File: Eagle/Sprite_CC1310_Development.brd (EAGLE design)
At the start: 50 x 50 mm, 81 parts, among them J2 CORTEX_DEBUG_SMD

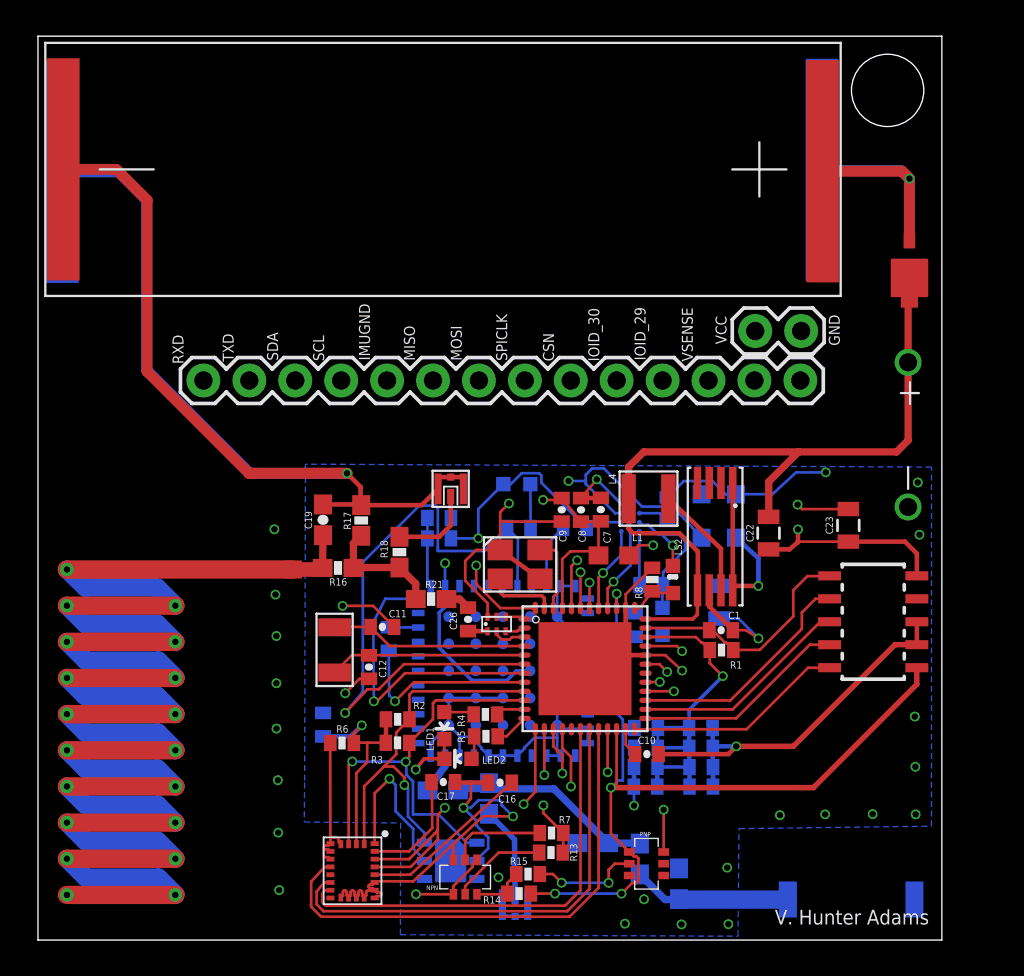
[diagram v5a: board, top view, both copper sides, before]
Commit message: RFQ for BSU, changed matching circuit
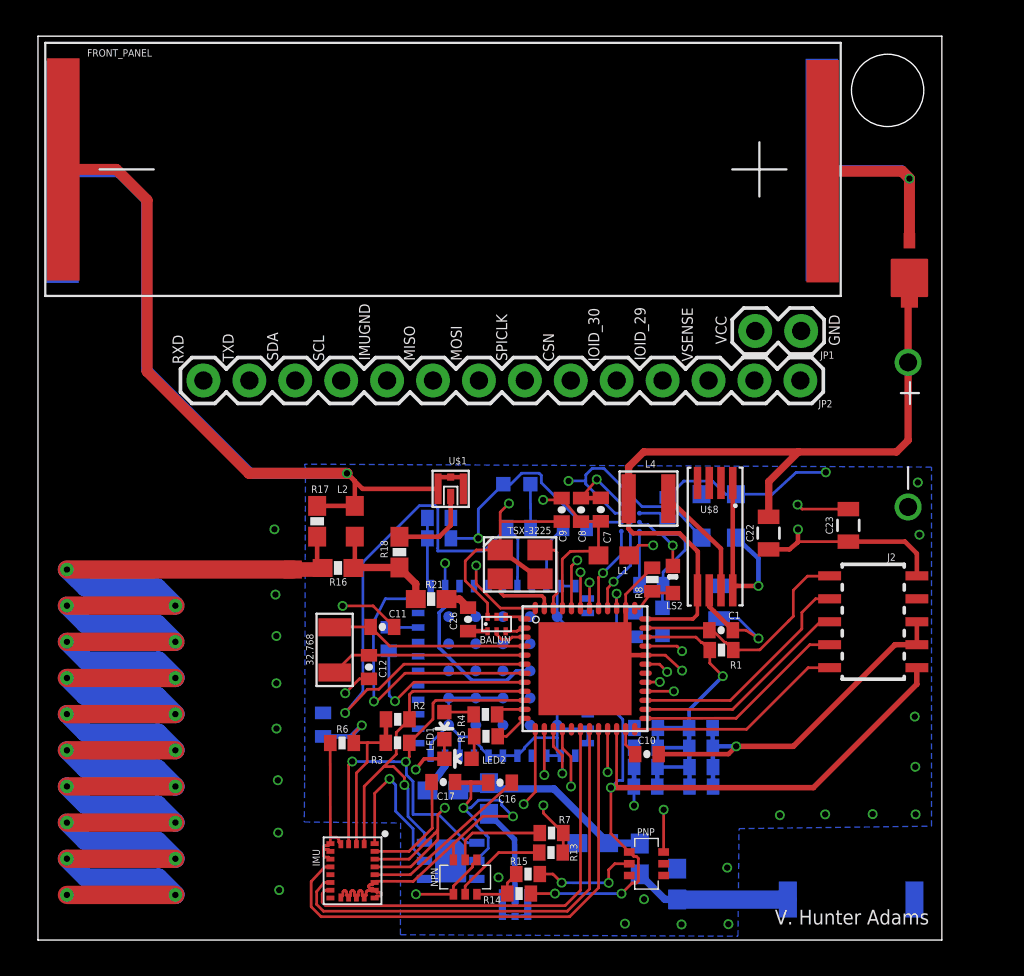
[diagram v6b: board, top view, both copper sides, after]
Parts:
- removed C19: 100pF, SparkFun:0603-CAP
- removed L3: 2.2 nH, SparkFun:0603
- added L2: 5.6nH, SparkFun:0603
- added R27: DNP, SparkFun:0603-RES
- moved R17 2.44 mm to (15.4, 23.2), turned to 270 degrees
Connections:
- net ANTENNA: now also R17.2; no longer C19.2
- net GND: now also L2.1, R17.1, R27.2; no longer C19.1, L3.1, R17.2
- net N$15: now also R27.1; no longer L3.2
- net N$26: now also L2.2; no longer R17.1
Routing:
- net GND: track 187.2 -> 187.8 mm
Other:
- board text added: "32.768"
- board text added: "BALUN"
- board text added: "FRONT_PANEL"
- board text added: "GPS"
- board text added: "IMU"
- board text added: "J2"
- board text added: "JP1"
- board text added: "JP2"
- board text added: "REAR_PANEL"
- board text added: "SI7021"
- board text added: "TSX-3225"
- board text added: "U$1"
- board text added: "U$2"
- board text added: "U$3"
- board text added: "U$4"
- board text added: "U$5"
- board text added: "U$8"

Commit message: BSU suggestions
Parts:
- added JP3: (no value), SparkFun:1X02
- added R28: 0, SparkFun:0603-RES
- moved SCHTOKKY 7.91 mm to (45.3, 29.7)
- moved C6 7.87 mm to (41.2, 14.0), turned to 180 degrees
- moved C2 5.91 mm to (41.2, 15.5)
- moved JP1 5.08 mm to (34.6, 33.7)
- moved C3 4.76 mm to (41.2, 12.3)
- moved C4 4.58 mm to (41.2, 10.6)
- moved C5 4.49 mm to (41.2, 8.90)
- moved C13 2.18 mm to (33.6, 12.8)
- moved REAR_PANEL 1.78 mm to (24.1, 42.5)
- moved FRONT_PANEL 1.73 mm to (24.1, 42.5)
- moved C14 1.37 mm to (33.6, 10.9)
- moved C15 0.56 mm to (33.6, 9.05)
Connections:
- new net N$51: R28.2, U$4.VCC
- net SOLAR_CELLS: now also JP3.1
- net SUPERCAP: now also JP3.2, R28.1
- net VDDS: no longer U$4.VCC
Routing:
- net SUPERCAP: track 42.3 -> 61.8 mm
- net SOLAR_CELLS: track 13.5 -> 28.1 mm
- net N$51: track 0.00 -> 6.52 mm
- net GND: track 187.8 -> 181.4 mm
- net VDDS: track 121.9 -> 119.2 mm
- net IMUGND: track 62.4 -> 64.6 mm
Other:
- board text added: "CTS"
- board text added: "IOID29"
- board text added: "RTS"
- board text removed: "GND"
- board text removed: "IOID_29"
- board text removed: "JP1"
- board text removed: "JP2"
- board text removed: "VCC"
